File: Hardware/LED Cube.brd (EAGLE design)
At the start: 160 x 100 mm, 223 parts, among them IC1 MEGA8-AI, IC10 FT232RL, IC11 FM24V10, IC12 MSGEQ7, IC14 MEGA32-A, IC2 74HC573D, IC3 74HC573D, IC4 74HC573D, IC5 74HC573D, IC6 74HC573D, IC7 74HC573D, IC8 74HC573D, IC9 74HC573D

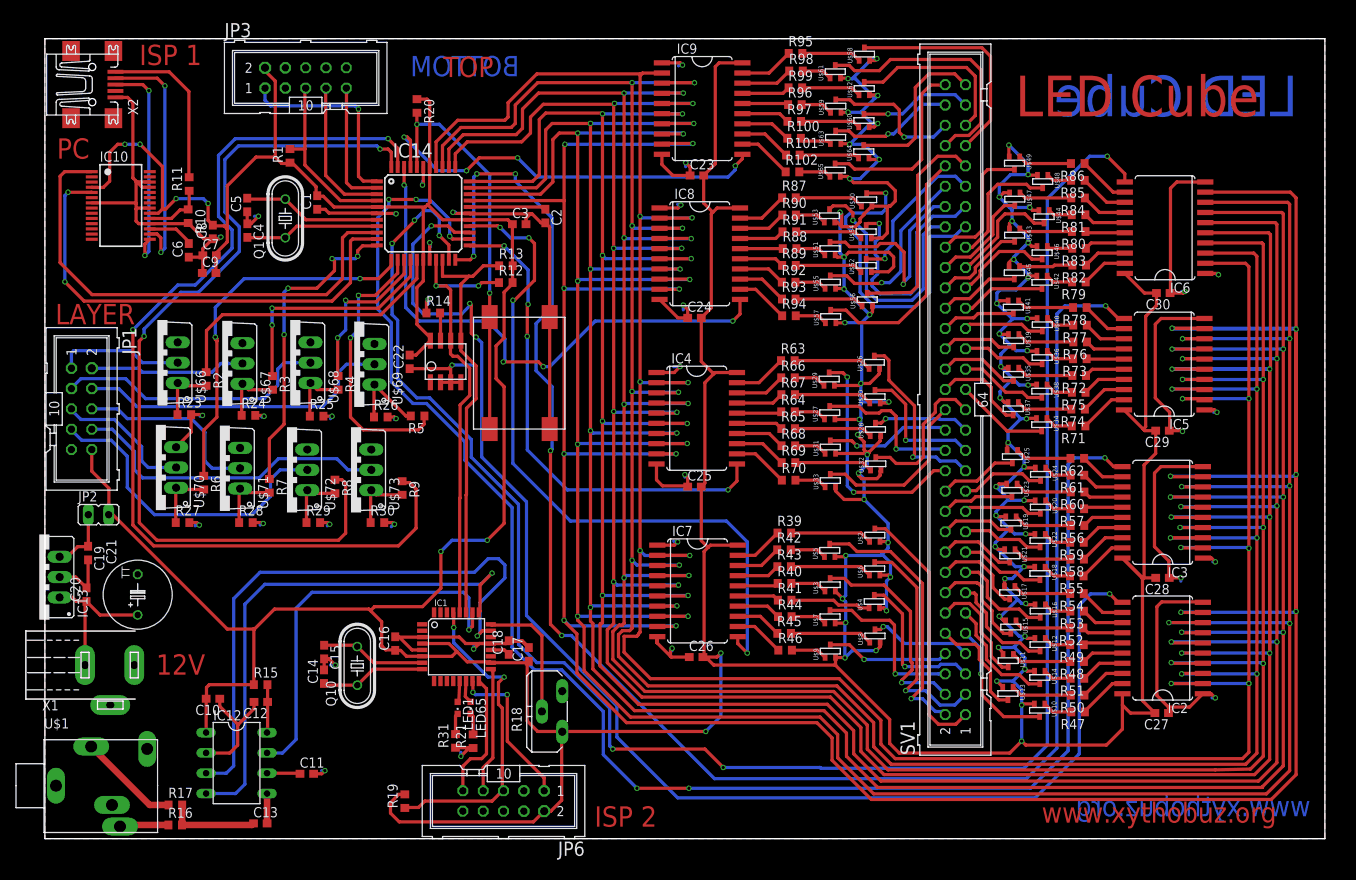
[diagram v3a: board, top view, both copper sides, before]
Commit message: Fixed Layout
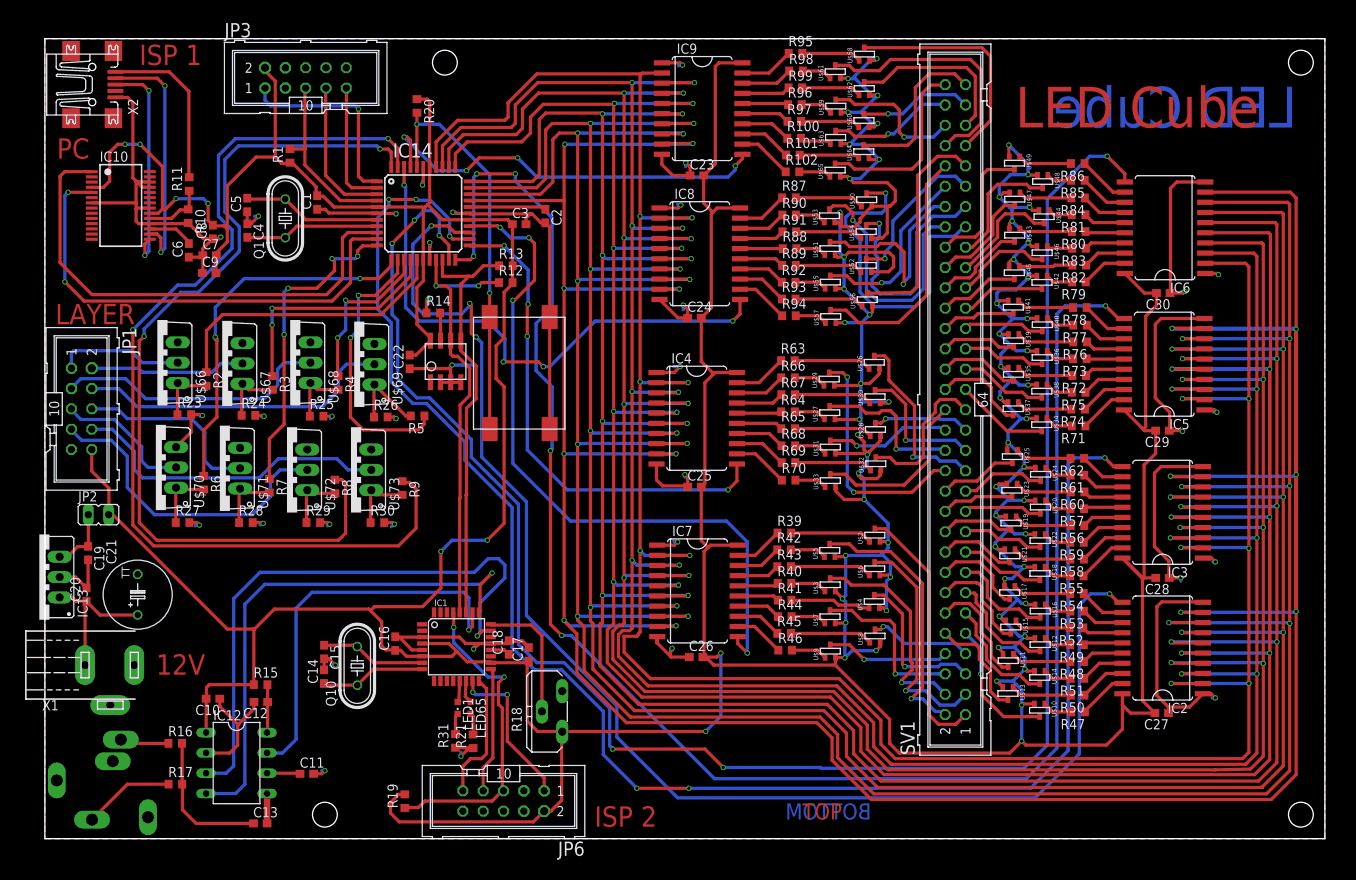
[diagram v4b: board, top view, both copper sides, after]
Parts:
- moved U$1 12.4 mm to (-0.01, 13.1), flipped to the bottom, turned to 180 degrees
- moved R16 10.2 mm to (16.3, 11.9)
- moved R17 2.60 mm to (16.3, 6.81)
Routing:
- net N$62: track 11.5 -> 17.9 mm
- net N$64: track 12.7 -> 11.4 mm
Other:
- board text removed: "www.xythobuz.org"
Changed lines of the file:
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@@
 <layer number="21" name="tPlace" color="7" fill="1" visible="yes" active="yes"/>
 <layer number="22" name="bPlace" color="7" fill="1" visible="yes" active="yes"/>
-<layer number="23" name="tOrigins" color="15" fill="1" visible="no" active="yes"/>
-<layer number="24" name="bOrigins" color="15" fill="1" visible="no" active="yes"/>
+<layer number="23" name="tOrigins" color="15" fill="1" visible="yes" active="yes"/>
+<layer number="24" name="bOrigins" color="15" fill="1" visible="yes" active="yes"/>
 <layer number="25" name="tNames" color="7" fill="1" visible="no" active="yes"/>
 <layer number="26" name="bNames" color="7" fill="1" visible="no" active="yes"/>
@@
 <layer number="43" name="vRestrict" color="2" fill="10" visible="yes" active="yes"/>
 <layer number="44" name="Drills" color="7" fill="1" visible="no" active="yes"/>
-<layer number="45" name="Holes" color="7" fill="1" visible="no" active="yes"/>
+<layer number="45" name="Holes" color="7" fill="1" visible="yes" active="yes"/>
 <layer number="46" name="Milling" color="3" fill="1" visible="no" active="yes"/>
 <layer number="47" name="Measures" color="7" fill="1" visible="yes" active="yes"/>
@@
 <wire x1="160" y1="100" x2="0" y2="100" width="0" layer="20"/>
 <wire x1="0" y1="100" x2="0" y2="0" width="0" layer="20"/>
-<text x="156.6" y="90.3" size="5.08" layer="16" font="vector" rot="MR0">LED Cube</text>
-<text x="158.2" y="2.8" size="2.54" layer="16" font="vector" rot="MR0">www.xythobuz.org</text>
-<text x="124.6" y="2" size="2.54" layer="1" font="vector">www.xythobuz.org</text>
-<text x="49.8" y="95.2" size="2.54" layer="1" font="vector">TOP</text>
-<text x="59.3" y="95.3" size="2.54" layer="16" font="vector" rot="MR0">BOTTOM</text>
-<text x="121.3" y="90.3" size="5.08" layer="1" font="vector">LED Cube</text>
+<text x="156.5" y="88.9" size="5.08" layer="16" font="vector" rot="MR0">LED Cube</text>
+<text x="94.7" y="2.4" size="2" layer="1" font="vector">TOP</text>
+<text x="103.3" y="2.4" size="2" layer="16" font="vector" rot="MR0">BOTTOM</text>
+<text x="121.3" y="88.9" size="5.08" layer="1" font="vector">LED Cube</text>
 <text x="68.7" y="1.5" size="2.54" layer="1" font="vector">ISP 2</text>
 <text x="11.8" y="96.7" size="2.54" layer="1" font="vector">ISP 1</text>
@@
 <text x="1.3" y="64.3" size="2.54" layer="1" font="vector">LAYER</text>
 <text x="13.9" y="20.5" size="2.54" layer="1" font="vector">12V</text>
+<hole x="157" y="97" drill="3.1"/>
+<hole x="157" y="3" drill="3.1"/>
+<hole x="50" y="97" drill="3.1"/>
+<hole x="35" y="3" drill="3.1"/>
 </plain>
 <attributes>
@@
 <element name="R15" library="resistor" package="R0603" value="200k" x="26.97" y="19.25"/>
 <element name="C13" library="resistor" package="C0603" value="10n" x="26.93" y="1.91"/>
-<element name="R16" library="resistor" package="R0603" value="200k" x="16.29" y="1.71"/>
-<element name="R17" library="resistor" package="R0603" value="200k" x="16.31" y="4.21"/>
+<element name="R16" library="resistor" package="R0603" value="200k" x="16.29" y="11.91"/>
+<element name="R17" library="resistor" package="R0603" value="200k" x="16.31" y="6.81"/>
 <element name="R20" library="resistor" package="R0603" value="1k" x="46.51" y="91.59" rot="R270"/>
 <element name="R19" library="resistor" package="R0603" value="10k" x="44.99" y="4.69" rot="R90"/>
@@
 </element>
 <element name="X2" library="1_USER" package="USB-B-MINI-SMD" value="" x="5.92" y="94.26"/>
-<element name="U$1" library="0-xythobuz" package="KLINKEPRINT" value="KLINKENBUCHSE" x="-0.11" y="0.77"/>
+<element name="U$1" library="0-xythobuz" package="KLINKEPRINT" value="KLINKENBUCHSE" x="-0.01" y="13.13" rot="MR180"/>
 <element name="LED1" library="led" package="CHIPLED_0603" value="" x="51.6" y="16.35" rot="R180"/>
 <element name="U$2" library="0-xythobuz" package="SOT323" value="PNP" x="103.74" y="37.79"/>
@@
 <contactref element="R16" pad="2"/>
 <contactref element="R17" pad="2"/>
-<wire x1="17.14" y1="1.71" x2="25.88" y2="1.71" width="0.8128" layer="1"/>
-<wire x1="25.88" y1="1.71" x2="26.08" y2="1.91" width="0.8128" layer="1"/>
-<wire x1="17.16" y1="4.21" x2="17.16" y2="1.73" width="0.8128" layer="1"/>
-<wire x1="17.16" y1="1.73" x2="17.14" y2="1.71" width="0.8128" layer="1"/>
+<wire x1="26.08" y1="1.91" x2="18.89" y2="1.91" width="0.4064" layer="1"/>
+<wire x1="18.89" y1="1.91" x2="17.2" y2="3.6" width="0.4064" layer="1"/>
+<wire x1="17.2" y1="3.6" x2="17.2" y2="6.77" width="0.4064" layer="1"/>
+<wire x1="17.2" y1="6.77" x2="17.16" y2="6.81" width="0.4064" layer="1"/>
+<wire x1="17.16" y1="6.81" x2="17.16" y2="11.89" width="0.4064" layer="1"/>
+<wire x1="17.16" y1="11.89" x2="17.14" y2="11.91" width="0.4064" layer="1"/>
 </signal>
 <signal name="N$63">
 <contactref element="R16" pad="1"/>
 <contactref element="U$1" pad="RIGHT"/>
-<wire x1="15.44" y1="1.71" x2="9.58" y2="1.71" width="0.8128" layer="1"/>
-<wire x1="9.58" y1="1.71" x2="9.39" y2="1.52" width="0.8128" layer="1"/>
+<wire x1="15.44" y1="11.91" x2="9.96" y2="11.91" width="0.4064" layer="1"/>
+<wire x1="9.96" y1="11.91" x2="9.49" y2="12.38" width="0.4064" layer="1"/>
 </signal>
 <signal name="N$64">
 <contactref element="R17" pad="1"/>
 <contactref element="U$1" pad="LEFT"/>
-<wire x1="15.46" y1="4.21" x2="13.1" y2="4.21" width="0.8128" layer="1"/>
-<wire x1="13.1" y1="4.21" x2="5.79" y2="11.52" width="0.8128" layer="1"/>
+<wire x1="15.46" y1="6.81" x2="10.32" y2="6.81" width="0.4064" layer="1"/>
+<wire x1="10.32" y1="6.81" x2="5.89" y2="2.38" width="0.4064" layer="1"/>
 </signal>
 <signal name="N$69">
